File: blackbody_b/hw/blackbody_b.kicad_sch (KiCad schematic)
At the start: 29 parts, among them IC101 TSL25911FN, J101 43650-0227, U101 NUCLEO-L432KC

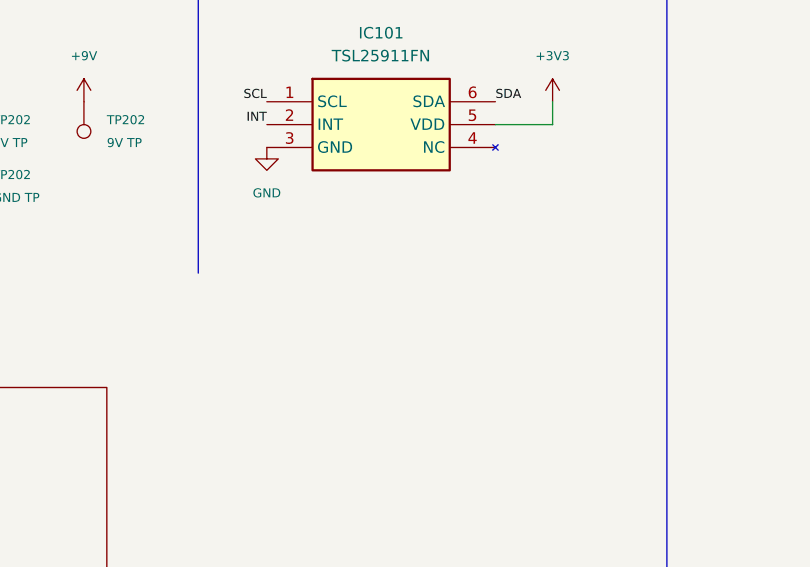
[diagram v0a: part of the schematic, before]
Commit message: fixes for blackbody b before prod
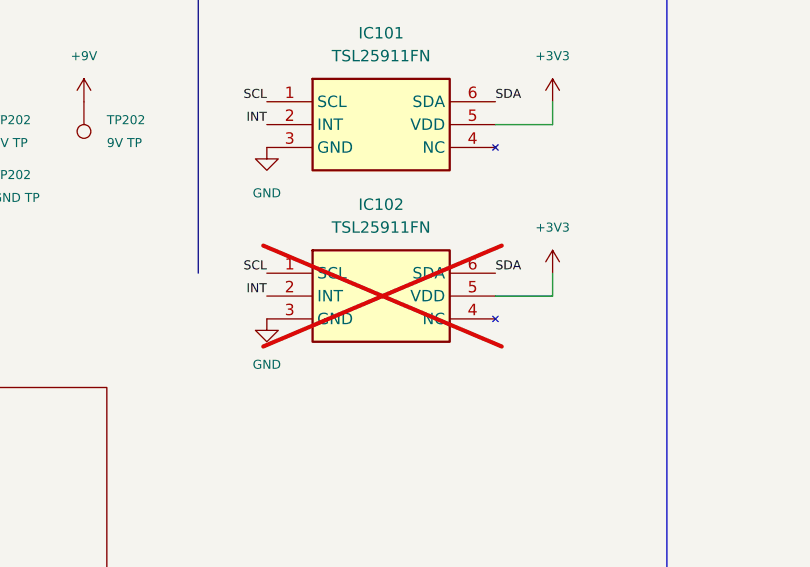
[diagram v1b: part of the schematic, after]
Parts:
- added IC102: TSL25911FN, footprints:ams_TSL25911FN, symbol ams_TSL25911FN:TSL25911FN
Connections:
- net +3V3: now also IC102.5 (VDD)
- net GND: now also IC102.3 (GND)
- net INT: now also IC102.2 (INT)
- net SCL: now also IC102.1 (SCL)
- net SDA: now also IC102.6 (SDA)
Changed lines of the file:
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@@
     (stroke (width 0) (type default))
   )
+  (wire (pts (xy 165.1 128.27) (xy 165.1 125.73))
+    (stroke (width 0) (type default))
+  )
   (wire (pts (xy 40.64 48.26) (xy 44.45 48.26))
     (stroke (width 0) (type default))
   )
+  (wire (pts (xy 158.75 128.27) (xy 165.1 128.27))
+    (stroke (width 0) (type default))
+  )
   (wire (pts (xy 88.9 36.83) (xy 96.52 36.83))
     (stroke (width 0) (type default))
@@
     (effects (font (size 1 1)) (justify right bottom))
   )
+  (label "INT" (at 133.35 128.27 180) (fields_autoplaced)
+    (effects (font (size 1 1)) (justify right bottom))
+  )
   (label "INT" (at 35.56 58.42 0) (fields_autoplaced)
     (effects (font (size 1 1)) (justify left bottom))
@@
     (effects (font (size 1 1)) (justify left bottom))
   )
+  (label "SDA" (at 158.75 125.73 0) (fields_autoplaced)
+    (effects (font (size 1 1)) (justify left bottom))
+  )
   (label "INT" (at 133.35 109.22 180) (fields_autoplaced)
     (effects (font (size 1 1)) (justify right bottom))
@@
     (effects (font (size 1 1)) (justify left bottom))
   )
+  (label "SCL" (at 133.35 125.73 180) (fields_autoplaced)
+    (effects (font (size 1 1)) (justify right bottom))
+  )
   (label "Heartbeat" (at 35.56 38.1 0) (fields_autoplaced)
     (effects (font (size 1 1)) (justify left bottom))
@@
     )
   )
+  (symbol (lib_id "power:GND") (at 133.35 130.81 0) (unit 1)
+    (in_bom yes) (on_board yes) (dnp no) (fields_autoplaced)
+    (property "Reference" "#PWR0118" (at 133.35 137.16 0)
+      (effects (font (size 1 1)) hide)
+    )
+    (property "Value" "GND" (at 133.35 135.89 0)
+      (effects (font (size 1 1)))
+    )
+    (property "Footprint" "" (at 133.35 130.81 0)
+      (effects (font (size 1 1)) hide)
+    )
+    (property "Datasheet" "" (at 133.35 130.81 0)
+      (effects (font (size 1 1)) hide)
+    )
+    (pin "1")
+    (instances
+      (project "blackbody_b"
+        (path "/6399d703-0339-4e9d-b32b-092bd33d8c6d"
+          (reference "#PWR0118") (unit 1)
+        )
+      )
+      (project "blackbody_a"
+        (path "/e2b99e66-bff9-4066-a55a-f270e38e89f4/9a2b4e12-b3ab-4fc6-b9c0-7a38a1eca447"
+          (reference "#PWR0204") (unit 1)
+        )
+      )
+    )
+  )
   (symbol (lib_id "Connector:TestPoint") (at 113.03 106.68 180) (unit 1)
     (in_bom yes) (on_board yes) (dnp no) (fields_autoplaced)
@@
   (symbol (lib_id "power:+3V3") (at 165.1 106.68 0) (unit 1)
     (in_bom yes) (on_board yes) (dnp no)
-    (property "Reference" "#PWR0118" (at 165.1 110.49 0)
+    (property "Reference" "#PWR0119" (at 165.1 110.49 0)
       (effects (font (size 1 1)) hide)
     )
@@
       (project "blackbody_b"
         (path "/6399d703-0339-4e9d-b32b-092bd33d8c6d"
-          (reference "#PWR0118") (unit 1)
+          (reference "#PWR0119") (unit 1)
         )
       )
@@
     )
   )
+  (symbol (lib_id "ams_TSL25911FN:TSL25911FN") (at 133.35 125.73 0) (unit 1)
+    (in_bom yes) (on_board yes) (dnp yes) (fields_autoplaced)
+    (property "Reference" "IC102" (at 146.05 118.11 0)
+      (effects (font (size 1.27 1.27)))
+    )
+    (property "Value" "TSL25911FN" (at 146.05 120.65 0)
+      (effects (font (size 1.27 1.27)))
+    )
+    (property "Footprint" "footprints:ams_TSL25911FN" (at 154.94 220.65 0)
+      (effects (font (size 1.27 1.27)) (justify left top) hide)
+    )
+    (property "Datasheet" "https://cdn-shop.adafruit.com/datasheets/TSL25911_Datasheet_EN_v1.pdf" (at 154.94 320.65 0)
+      (effects (font (size 1.27 1.27)) (justify left top) hide)
+    )
+    (property "Distributor" "Mouser" (at 133.35 125.73 0)
+      (effects (font (size 1.27 1.27)) hide)
+    )
+    (property "Manufacturer" "AMS" (at 133.35 125.73 0)
+      (effects (font (size 1.27 1.27)) hide)
+    )
+    (property "P/N" "TSL25911FN" (at 133.35 125.73 0)
+      (effects (font (size 1.27 1.27)) hide)
+    )
+    (property "LCSC Part #" "" (at 133.35 125.73 0)
+      (effects (font (size 1.27 1.27)) hide)
+    )
+    (property "Cost" "2.93" (at 133.35 125.73 0)
+      (effects (font (size 1.27 1.27)) hide)
+    )
+    (property "Notes" "" (at 133.35 125.73 0)
+      (effects (font (size 1.27 1.27)) hide)
+    )
+    (pin "1")
+    (pin "2")
+    (pin "3")
+    (pin "4")
+    (pin "5")
+    (pin "6")
+    (instances
+      (project "blackbody_b"
+        (path "/6399d703-0339-4e9d-b32b-092bd33d8c6d"
+          (reference "IC102") (unit 1)
+        )
+      )
+    )
+  )
   (symbol (lib_id "Device:C_Small") (at 88.9 39.37 0) (unit 1)
     (in_bom yes) (on_board yes) (dnp no) (fields_autoplaced)
@@
         )
       )
+    )
+  )
+  (symbol (lib_id "power:+3V3") (at 165.1 125.73 0) (unit 1)
+    (in_bom yes) (on_board yes) (dnp no)
+    (property "Reference" "#PWR0120" (at 165.1 129.54 0)
+      (effects (font (size 1 1)) hide)
+    )
+    (property "Value" "+3V3" (at 165.1 120.65 0)
+      (effects (font (size 1 1)))
+    )
+    (property "Footprint" "" (at 165.1 125.73 0)
+      (effects (font (size 1 1)) hide)
+    )
+    (property "Datasheet" "" (at 165.1 125.73 0)
+      (effects (font (size 1 1)) hide)
+    )
+    (pin "1")
+    (instances
+      (project "blackbody_b"
+        (path "/6399d703-0339-4e9d-b32b-092bd33d8c6d"
+          (reference "#PWR0120") (unit 1)
+        )
+      )
+      (project "blackbody_a"
+        (path "/e2b99e66-bff9-4066-a55a-f270e38e89f4"
+          (reference "#PWR015") (unit 1)
+        )
+        (path "/e2b99e66-bff9-4066-a55a-f270e38e89f4/9a2b4e12-b3ab-4fc6-b9c0-7a38a1eca447"
+          (reference "#PWR0205") (unit 1)
+        )
+        (path "/e2b99e66-bff9-4066-a55a-f270e38e89f4/ca469639-9f09-4f9d-ad48-0cec812f9eb6"
+          (reference "#PWR01106") (unit 1)
+        )
+      )
